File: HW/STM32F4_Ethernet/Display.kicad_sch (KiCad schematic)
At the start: 15 parts, among them J3 Conn_01x14

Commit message: Progress backup
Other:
- note added: "1 C2P 2 C2N 3 C1P 4 C1N 5 VBAT 6 VBREF(NC) 7 VSS 8 VDD 9 RES# 10 SCL 11 SDA 12 IREF 13 VCOMH 14 VCC"
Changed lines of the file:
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@@
     (stroke (width 0) (type default) (color 0 0 0 0))
+  )
+  (text "1   C2P\n2   C2N\n3   C1P\n4   C1N\n5   VBAT\n6   VBREF(NC)\n7   VSS\n8   VDD\n9   RES#\n10  SCL\n11  SDA\n12  IREF\n13  VCOMH\n14  VCC"
+    (at 171.45 99.06 0)
+    (effects (font (size 1.5 1.5)) (justify left bottom))
   )
   (text "I2C Pull-up" (at 247.65 67.31 0)
@@
   )
   (symbol (lib_id "Connector_Generic:Conn_01x14") (at 166.37 81.28 0) (unit 1)
-    (in_bom yes) (on_board yes) (fields_autoplaced)
-    (property "Reference" "J3" (id 0) (at 168.91 81.2799 0)
-      (effects (font (size 1.27 1.27)) (justify left))
-    )
-    (property "Value" "Conn_01x14" (id 1) (at 168.91 83.8199 0)
-      (effects (font (size 1.27 1.27)) (justify left))
-    )
+    (in_bom yes) (on_board yes)
+    (property "Reference" "J3" (id 0) (at 165.1 102.87 0)
+      (effects (font (size 1.27 1.27)) (justify left))
+    )
+    (property "Value" "Conn_01x14" (id 1) (at 165.1 105.41 0)
+      (effects (font (size 1.27 1.27)) (justify left))
+    )

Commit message: Progress backup. add SRAM
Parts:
- gave numbers to parts that had none: 14

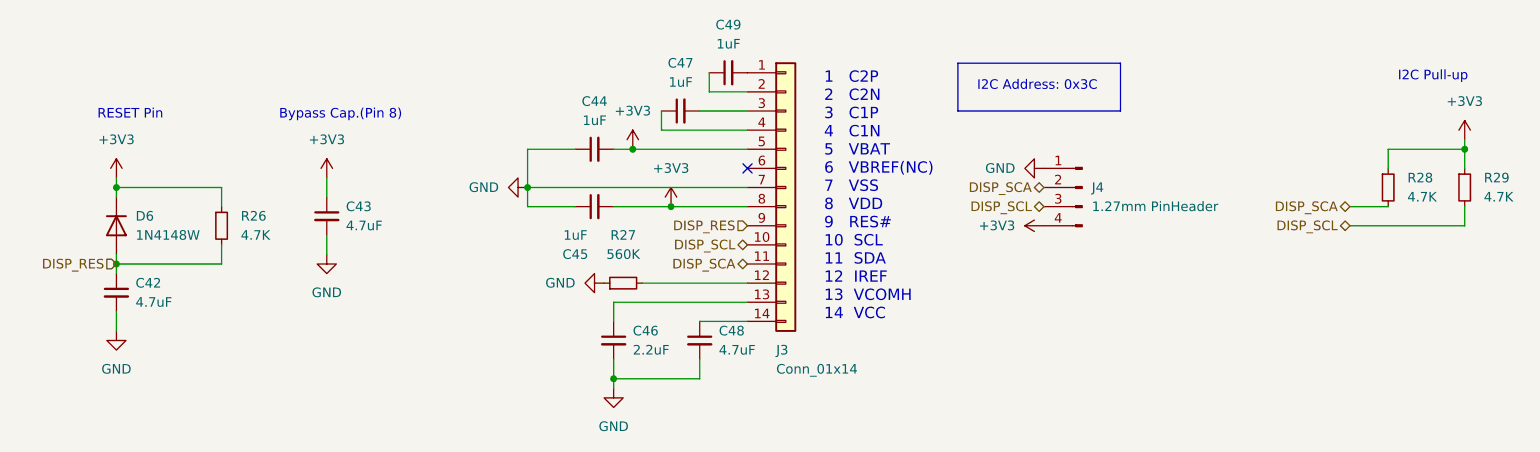
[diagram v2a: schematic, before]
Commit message: Sample PCB. Need to update RLC Size
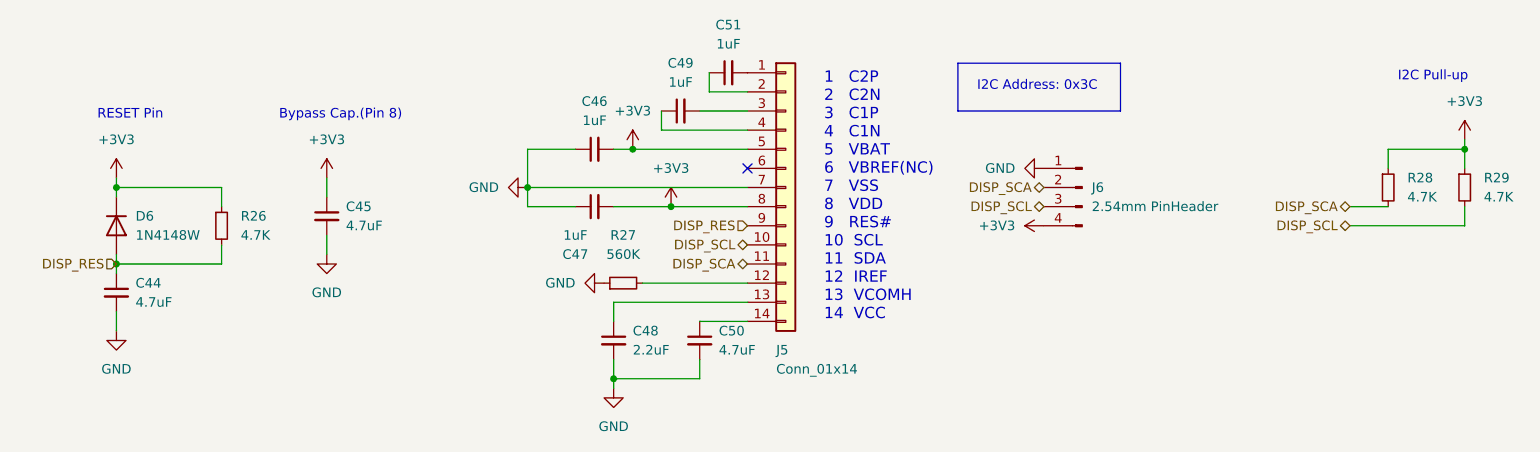
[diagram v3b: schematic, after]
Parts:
- C44: renamed from C42; footprint (none) -> Capacitor_SMD:C_0603_1608Metric_Pad1.08x0.95mm_HandSolder
- C45: renamed from C43; footprint (none) -> Capacitor_SMD:C_0603_1608Metric_Pad1.08x0.95mm_HandSolder
- C46: renamed from C44; footprint (none) -> Capacitor_SMD:C_0603_1608Metric_Pad1.08x0.95mm_HandSolder
- C47: renamed from C45; footprint (none) -> Capacitor_SMD:C_0603_1608Metric_Pad1.08x0.95mm_HandSolder
- C48: renamed from C46; footprint (none) -> Capacitor_SMD:C_0603_1608Metric_Pad1.08x0.95mm_HandSolder
- C49: renamed from C47; footprint (none) -> Capacitor_SMD:C_0603_1608Metric_Pad1.08x0.95mm_HandSolder
- C50: renamed from C48; footprint (none) -> Capacitor_SMD:C_0603_1608Metric_Pad1.08x0.95mm_HandSolder
- C51: renamed from C49; footprint (none) -> Capacitor_SMD:C_0603_1608Metric_Pad1.08x0.95mm_HandSolder
- J6: renamed from J4; value 1.27mm PinHeader -> 2.54mm PinHeader; footprint (none) -> Connector_PinHeader_2.54mm:PinHeader_1x04_P2.54mm_Vertical
- R26, R27, R28, R29: footprint (none) -> Resistor_SMD:R_0603_1608Metric_Pad0.98x0.95mm_HandSolder
- renumbered J3 to J5
